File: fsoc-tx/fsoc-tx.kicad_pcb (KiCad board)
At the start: 4 copper layers, 52 x 40 mm, 52 parts, among them J1 USB4105-GF-A, J2 B8B-PH-K-S, J3 FTSH-105-01-L-DV-K, J4 B3B-PH-K-S, J5 Conn_01x03, SW1 SW_RESET, SW2 USB_BOOT, SW3 SW_DPST, U1 USBLC6-2SC6, U2 AP2112K-3.3, U3 RP2354A, U4 74AHCT1G125, U5 TPS22919DCK, Y1 ABM8-272-T3, Y2 ASTX-H11-10.000MHz-T

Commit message: TX PCB: DONE
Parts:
- J1: footprint Connector_USB:USB_C_Receptacle_GCT_USB4105-xx-A_16P_TopMnt_Horizontal -> fsoc_footprints:TYPE-C-31-M-14
- moved J1 2.44 mm to (150.9, 106.0)
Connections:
- net /USB_DM renamed /USB_DN
- net Net-(J1-D+-PadA6) renamed /TX_POWER_USB/USB_CONN_DP
- net Net-(J1-D--PadA7) renamed /TX_POWER_USB/USB_CONN_DN
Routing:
- net GND: track 102.7 -> 98.5 mm, vias 53 -> 47
- net /TX_POWER_USB/USB_CONN_DP: track 11.3 -> 13.0 mm
- net /USB_DN: track 2.87 -> 4.38 mm
- net Net-(J1-CC2): track 4.43 -> 5.76 mm
- net /TX_POWER_USB/USB_CONN_DN: track 11.2 -> 12.1 mm
- net Net-(J1-CC1): track 3.20 -> 4.13 mm
- net /TX_POWER_USB/VBUS_USB: track 42.9 -> 43.6 mm, vias 0 -> 2
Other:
- board size 52 x 40 mm -> 52.1 x 40 mm

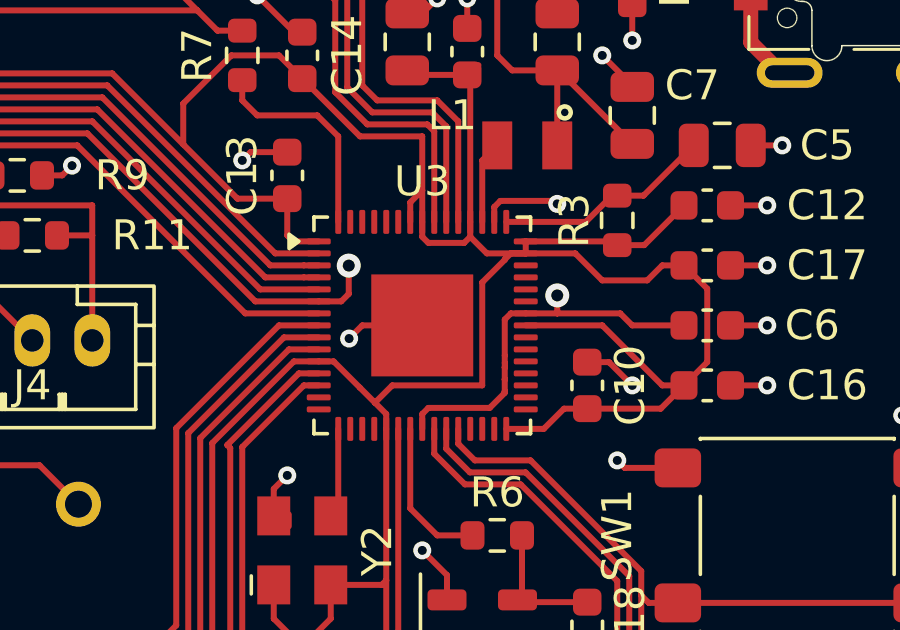
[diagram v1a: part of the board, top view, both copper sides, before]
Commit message: TX PCB: U3 footprint changed to the thermal vias version
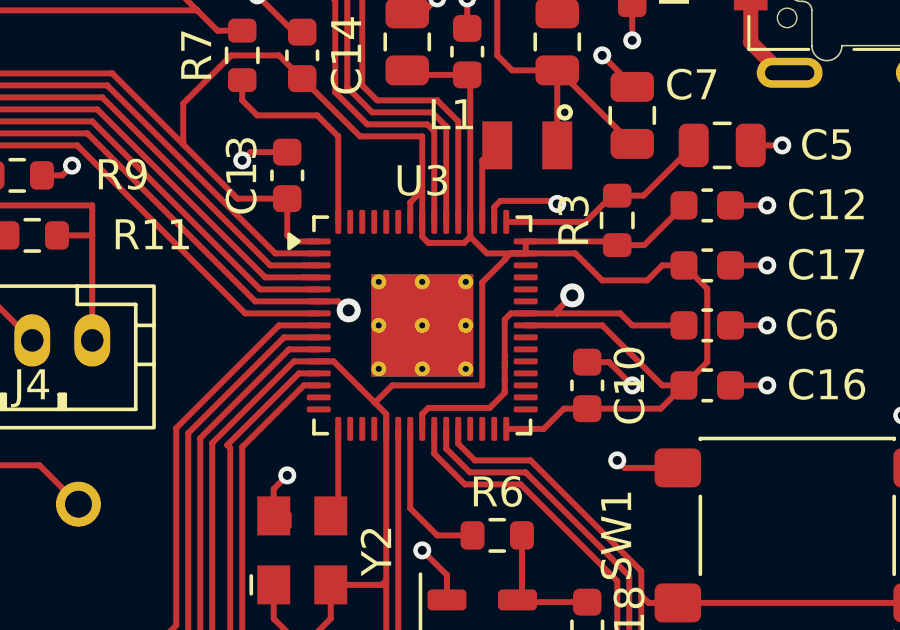
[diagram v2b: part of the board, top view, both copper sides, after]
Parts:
- U3: footprint Package_DFN_QFN:QFN-60-1EP_7x7mm_P0.4mm_EP3.4x3.4mm -> Package_DFN_QFN:QFN-60-1EP_7x7mm_P0.4mm_EP3.4x3.4mm_ThermalVias
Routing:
- net /TX_MCU_CLOCK/+1V1: track 84.1 -> 87.0 mm
- net GND: track 98.5 -> 95.9 mm, vias 47 -> 46
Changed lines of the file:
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@@
 		)
 	)
-	(footprint "Package_DFN_QFN:QFN-60-1EP_7x7mm_P0.4mm_EP3.4x3.4mm"
+	(footprint "Package_DFN_QFN:QFN-60-1EP_7x7mm_P0.4mm_EP3.4x3.4mm_ThermalVias"
 		(layer "F.Cu")
 		(at 135 120)
@@
 		)
 		(pad "" smd roundrect
-			(at -1.13 -1.13)
-			(size 0.91 0.91)
+			(at -0.85 -0.85)
+			(size 1.32 1.32)
 			(layers "F.Paste")
-			(roundrect_rratio 0.25)
-		)
-		(pad "" smd roundrect
-			(at -1.13 0)
-			(size 0.91 0.91)
-			(layers "F.Paste")
-			(roundrect_rratio 0.25)
-		)
-		(pad "" smd roundrect
-			(at -1.13 1.13)
-			(size 0.91 0.91)
-			(layers "F.Paste")
-			(roundrect_rratio 0.25)
-		)
-		(pad "" smd roundrect
-			(at 0 -1.13)
-			(size 0.91 0.91)
-			(layers "F.Paste")
-			(roundrect_rratio 0.25)
-		)
-		(pad "" smd roundrect
-			(at 0 0)
-			(size 0.91 0.91)
-			(layers "F.Paste")
-			(roundrect_rratio 0.25)
-		)
-		(pad "" smd roundrect
-			(at 0 1.13)
-			(size 0.91 0.91)
-			(layers "F.Paste")
-			(roundrect_rratio 0.25)
+			(roundrect_rratio 0.189394)
 		)
 		(pad "" smd roundrect
-			(at 1.13 -1.13)
-			(size 0.91 0.91)
+			(at -0.85 0.85)
+			(size 1.32 1.32)
 			(layers "F.Paste")
-			(roundrect_rratio 0.25)
+			(roundrect_rratio 0.189394)
 		)
 		(pad "" smd roundrect
-			(at 1.13 0)
-			(size 0.91 0.91)
+			(at 0.85 -0.85)
+			(size 1.32 1.32)
 			(layers "F.Paste")
-			(roundrect_rratio 0.25)
+			(roundrect_rratio 0.189394)
 		)
 		(pad "" smd roundrect
-			(at 1.13 1.13)
-			(size 0.91 0.91)
+			(at 0.85 0.85)
+			(size 1.32 1.32)
 			(layers "F.Paste")
-			(roundrect_rratio 0.25)
+			(roundrect_rratio 0.189394)
 		)
 		(pad "1" smd roundrect
@@
 			(pintype "output")
 		)
+		(pad "61" thru_hole circle
+			(at -1.45 -1.45)
+			(size 0.5 0.5)
+			(drill 0.2)
+			(property pad_prop_heatsink)
+			(layers "*.Cu")
+			(remove_unused_layers no)
+			(net "GND")
+			(pinfunction "GND_61")
+			(pintype "power_in")
+		)
+		(pad "61" thru_hole circle
+			(at -1.45 0)
+			(size 0.5 0.5)
+			(drill 0.2)
+			(property pad_prop_heatsink)
+			(layers "*.Cu")
+			(remove_unused_layers no)
+			(net "GND")
+			(pinfunction "GND_61")
+			(pintype "power_in")
+		)
+		(pad "61" thru_hole circle
+			(at -1.45 1.45)
+			(size 0.5 0.5)
+			(drill 0.2)
+			(property pad_prop_heatsink)
+			(layers "*.Cu")
+			(remove_unused_layers no)
+			(net "GND")
+			(pinfunction "GND_61")
+			(pintype "power_in")
+		)
+		(pad "61" thru_hole circle
+			(at 0 -1.45)
+			(size 0.5 0.5)
+			(drill 0.2)
+			(property pad_prop_heatsink)
+			(layers "*.Cu")
+			(remove_unused_layers no)
+			(net "GND")
+			(pinfunction "GND_61")
+			(pintype "power_in")
+		)
+		(pad "61" thru_hole circle
+			(at 0 0)
+			(size 0.5 0.5)
+			(drill 0.2)
+			(property pad_prop_heatsink)
+			(layers "*.Cu")
+			(remove_unused_layers no)
+			(net "GND")
+			(pinfunction "GND_61")
+			(pintype "power_in")
+		)
 		(pad "61" smd rect
 			(at 0 0)
@@
 			(zone_connect 2)
 		)
+		(pad "61" smd rect
+			(at 0 0)
+			(size 3.4 3.4)
+			(property pad_prop_heatsink)
+			(layers "B.Cu")
+			(net "GND")
+			(pinfunction "GND_61")
+			(pintype "power_in")
+			(zone_connect 2)
+		)
+		(pad "61" thru_hole circle
+			(at 0 1.45)
+			(size 0.5 0.5)
+			(drill 0.2)
+			(property pad_prop_heatsink)
+			(layers "*.Cu")
+			(remove_unused_layers no)
+			(net "GND")
+			(pinfunction "GND_61")
+			(pintype "power_in")
+		)
+		(pad "61" thru_hole circle
+			(at 1.45 -1.45)
+			(size 0.5 0.5)
+			(drill 0.2)
+			(property pad_prop_heatsink)
+			(layers "*.Cu")
+			(remove_unused_layers no)
+			(net "GND")
+			(pinfunction "GND_61")
+			(pintype "power_in")
+		)
+		(pad "61" thru_hole circle
+			(at 1.45 0)
+			(size 0.5 0.5)
+			(drill 0.2)
+			(property pad_prop_heatsink)
+			(layers "*.Cu")
+			(remove_unused_layers no)
+			(net "GND")
+			(pinfunction "GND_61")
+			(pintype "power_in")
+		)
+		(pad "61" thru_hole circle
+			(at 1.45 1.45)
+			(size 0.5 0.5)
+			(drill 0.2)
+			(property pad_prop_heatsink)
+			(layers "*.Cu")
+			(remove_unused_layers no)
+			(net "GND")
+			(pinfunction "GND_61")
+			(pintype "power_in")
+		)
 		(embedded_fonts no)
 		(model "${KICAD10_3DMODEL_DIR}/Package_DFN_QFN.3dshapes/QFN-60-1EP_7x7mm_P0.4mm_EP3.4x3.4mm.step"
@@
 	)
 	(segment
-		(start 132.562089 120.437911)
-		(end 133 120)
-		(width 0.2)
-		(layer "F.Cu")
-		(net "GND")
-	)
-	(segment
 		(start 145.95 101.483946)
 		(end 147.083946 100.35)
@@
 	)
 	(segment
-		(start 133 120)
-		(end 135 120)
-		(width 0.2)
-		(layer "F.Cu")
-		(net "GND")
-	)
-	(segment
 		(start 141.225 121.225)
 		(end 142 122)
@@
 	)
 	(via
-		(at 132.562089 120.437911)
-		(size 0.6)
-		(drill 0.3)
-		(layers "F.Cu" "B.Cu")
-		(net "GND")
-	)
-	(via
 		(at 147 114)
 		(size 0.6)
@@
 	)
 	(segment
-		(start 132.3 119.2)
-		(end 131.55 119.2)
-		(width 0.2)
-		(layer "F.Cu")
-		(net "/TX_MCU_CLOCK/+1V1")
-	)
-	(segment
 		(start 137.75364 121.4)
 		(end 137.75 121.39636)
@@
 	)
 	(segment
-		(start 132.55 118.95)
-		(end 132.3 119.2)
-		(width 0.2)
-		(layer "F.Cu")
-		(net "/TX_MCU_CLOCK/+1V1")
-	)
-	(segment
 		(start 137.75364 122.2)
 		(end 137.75 122.19636)
@@
 	)
 	(segment
+		(start 132.501163 119.498837)
+		(end 132.548216 119.498837)
+		(width 0.2)
+		(layer "F.Cu")
+		(net "/TX_MCU_CLOCK/+1V1")
+	)
+	(segment
 		(start 131.55 119.2)
 		(end 129.437256 119.2)
@@
 	)
 	(segment
+		(start 132.5 119.5)
+		(end 132.501163 119.498837)
+		(width 0.2)
+		(layer "F.Cu")
+		(net "/TX_MCU_CLOCK/+1V1")
+	)
+	(segment
 		(start 133.5 112.5)
 		(end 133 112)
@@
 	)
 	(segment
-		(start 139.5 119.6)
-		(end 139.5 119)
+		(start 131.55 119.2)
+		(end 132.2 119.2)
 		(width 0.2)
 		(layer "F.Cu")
@@
 	)
 	(segment
+		(start 139.5 119.5)
+		(end 140 119)
+		(width 0.2)
+		(layer "F.Cu")
+		(net "/TX_MCU_CLOCK/+1V1")
+	)
+	(segment
+		(start 132.2 119.2)
+		(end 132.5 119.5)
+		(width 0.2)
+		(layer "F.Cu")
+		(net "/TX_MCU_CLOCK/+1V1")
+	)
+	(segment
 		(start 133 109)
 		(end 133.5 108.5)
@@
 	)
 	(segment
+		(start 139.5 119.6)
+		(end 139.5 119.5)
+		(width 0.2)
+		(layer "F.Cu")
+		(net "/TX_MCU_CLOCK/+1V1")
+	)
+	(segment
 		(start 137.75 121.40364)
 		(end 137.75364 121.4)
@@
 	)
 	(segment
-		(start 132.55 118.006761)
-		(end 132.55 118.95)
-		(width 0.2)
-		(layer "F.Cu")
-		(net "/TX_MCU_CLOCK/+1V1")
-	)
-	(segment
 		(start 137.75 122.19636)
 		(end 137.75 121.80364)
@@
 	)
 	(via
-		(at 139.5 119)
+		(at 132.548216 119.498837)
 		(size 0.8)
 		(drill 0.4)
@@
 	)
 	(via
-		(at 132.55 118.006761)
+		(at 140 119)
 		(size 0.8)
 		(drill 0.4)
@@
 	)
 	(segment
-		(start 133.5 118)
-		(end 132.556761 118)
+		(start 132.548216 115)
+		(end 132.548216 108.451784)
 		(width 0.5)
 		(layer "In2.Cu")
@@
 	)
 	(segment
-		(start 132.556761 118)
-		(end 132.55 118.006761)
+		(start 132.548216 108.451784)
+		(end 133.5 107.5)
 		(width 0.5)
 		(layer "In2.Cu")
@@
 	)
 	(segment
-		(start 133.5 118)
-		(end 138.5 118)
+		(start 132.548216 119.498837)
+		(end 132.548216 115)
 		(width 0.5)
 		(layer "In2.Cu")
@@
 	)
 	(segment
-		(start 138.5 118)
-		(end 139.5 119)
+		(start 136 115)
+		(end 140 119)
 		(width 0.5)
 		(layer "In2.Cu")
@@
 	)
 	(segment
-		(start 133.5 107.5)
-		(end 133.5 118)
+		(start 132.548216 115)
+		(end 136 115)
 		(width 0.5)
 		(layer "In2.Cu")

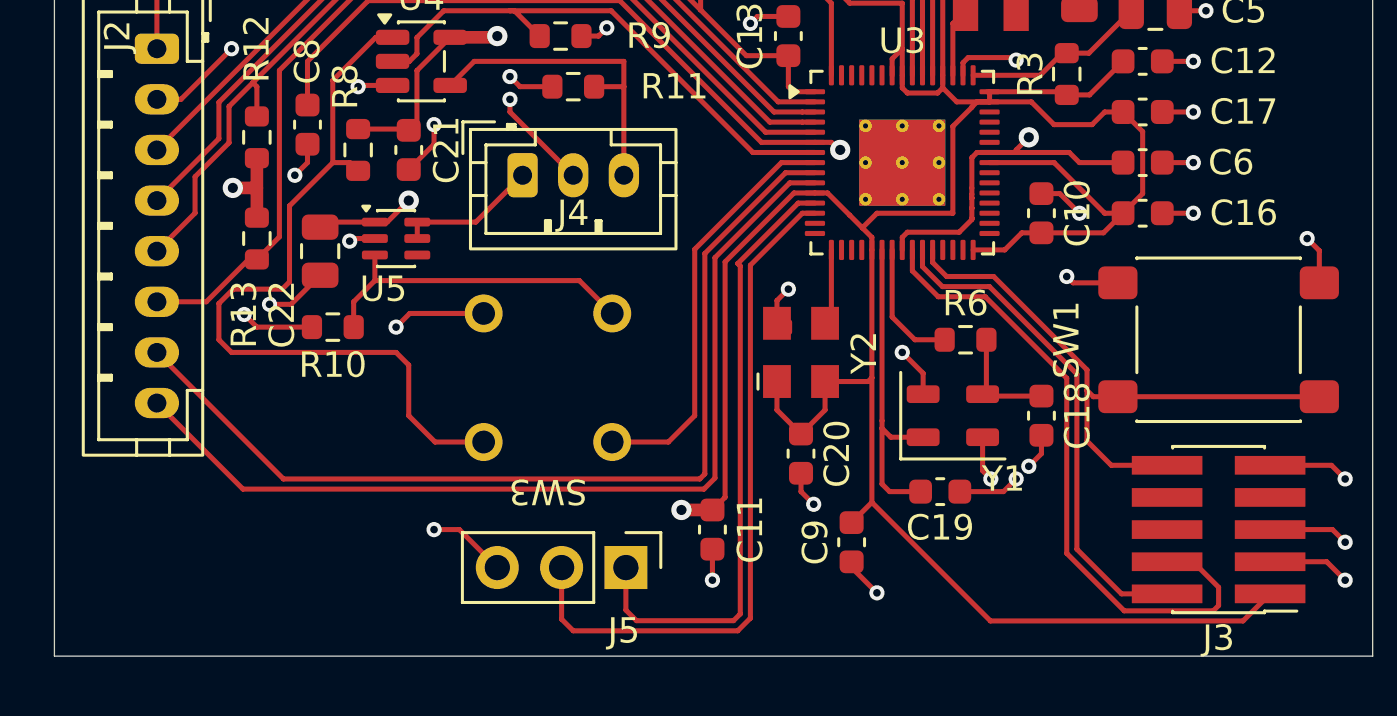
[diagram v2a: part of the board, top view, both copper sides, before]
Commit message: Switching ASTX-H11 to SiT5346 and SiT5346 datasheet
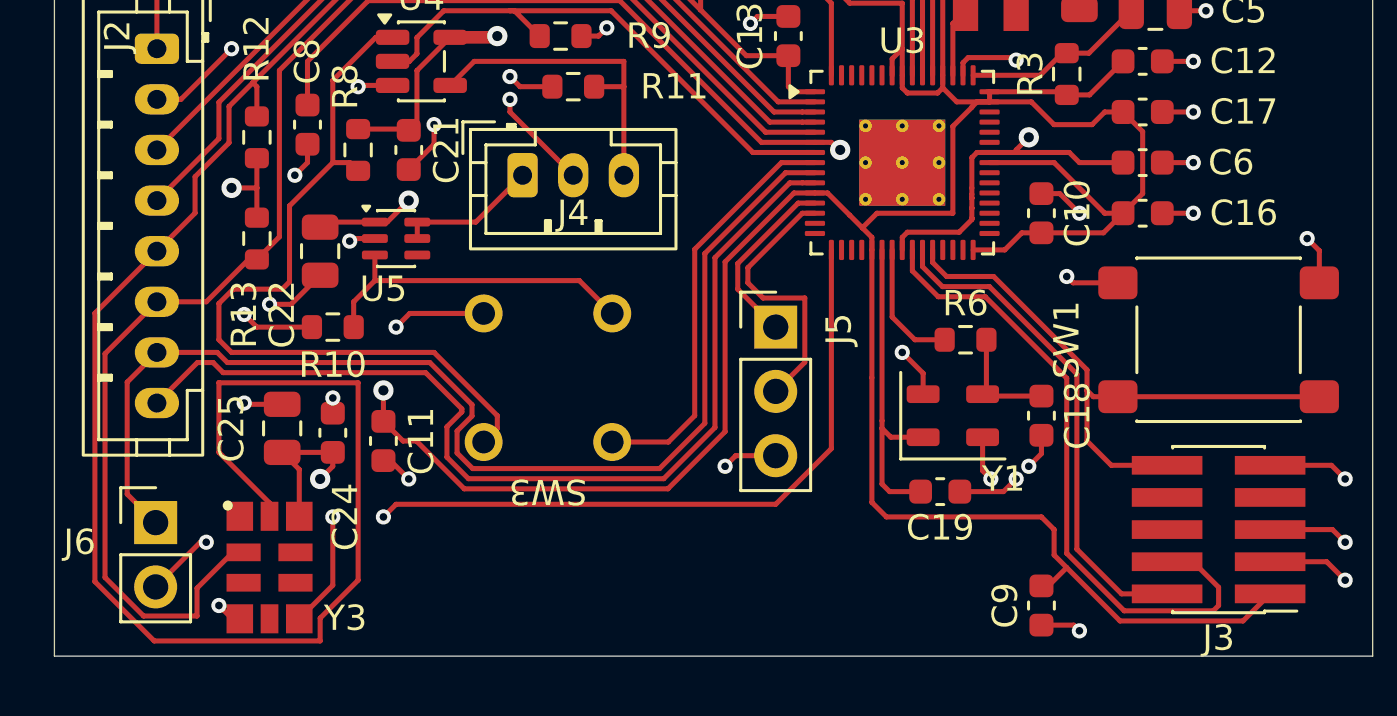
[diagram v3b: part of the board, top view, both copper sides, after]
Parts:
- removed C20: 10 nF, Capacitor_SMD:C_0603_1608Metric
- removed Y2: ASTX-H11-10.000MHz-T, fsoc_footprints:ASTX-H11_3225
- added C24: 100 nF, Capacitor_SMD:C_0603_1608Metric, F.Cu at (112.5, 130.7)
- added C25: 10 µF, Capacitor_SMD:C_0805_2012Metric, F.Cu at (110.5, 130.5)
- added J6: Conn_01x02, Connector_PinHeader_2.54mm:PinHeader_1x02_P2.54mm_Vertical, F.Cu at (105.5, 134.2)
- added Y3: SiT5346, fsoc_footprints:SiT5346_5.0x3.2mm_10L, F.Cu at (110.0, 136.0)
- moved C11 13.5 mm to (114.5, 131.0)
- moved J5 11.2 mm to (130.0, 126.5), turned to 0 degrees
- moved C9 7.91 mm to (140.5, 137.5)
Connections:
- U3 pad 16: /TX_MCU_CLOCK/TCXO_10M -> /TX_MCU_CLOCK/REF_10M
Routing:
- net /HOST_I2C_SDA: track 35.8 -> 82.2 mm
- net /TX_MCU_CLOCK/REF_10M: track 0.00 -> 33.2 mm, vias 0 -> 2
- net /HOST_I2C_SCL: track 37.3 -> 56.8 mm
- net /UART_DEBUG_TX: track 24.4 -> 7.17 mm
- net /UART_DEBUG_RX: track 27.2 -> 10.8 mm
- net /PPS_OUT: track 38.2 -> 46.3 mm
- net /TX_MCU_CLOCK/TCXO_10M: track 3.00 -> 0.00 mm
- net /+3V3_DIG: track 180.2 -> 177.9 mm, vias 2 -> 3
- net /HOST_READY: track 38.0 -> 39.7 mm
- net GND: track 95.9 -> 97.3 mm, vias 46 -> 48

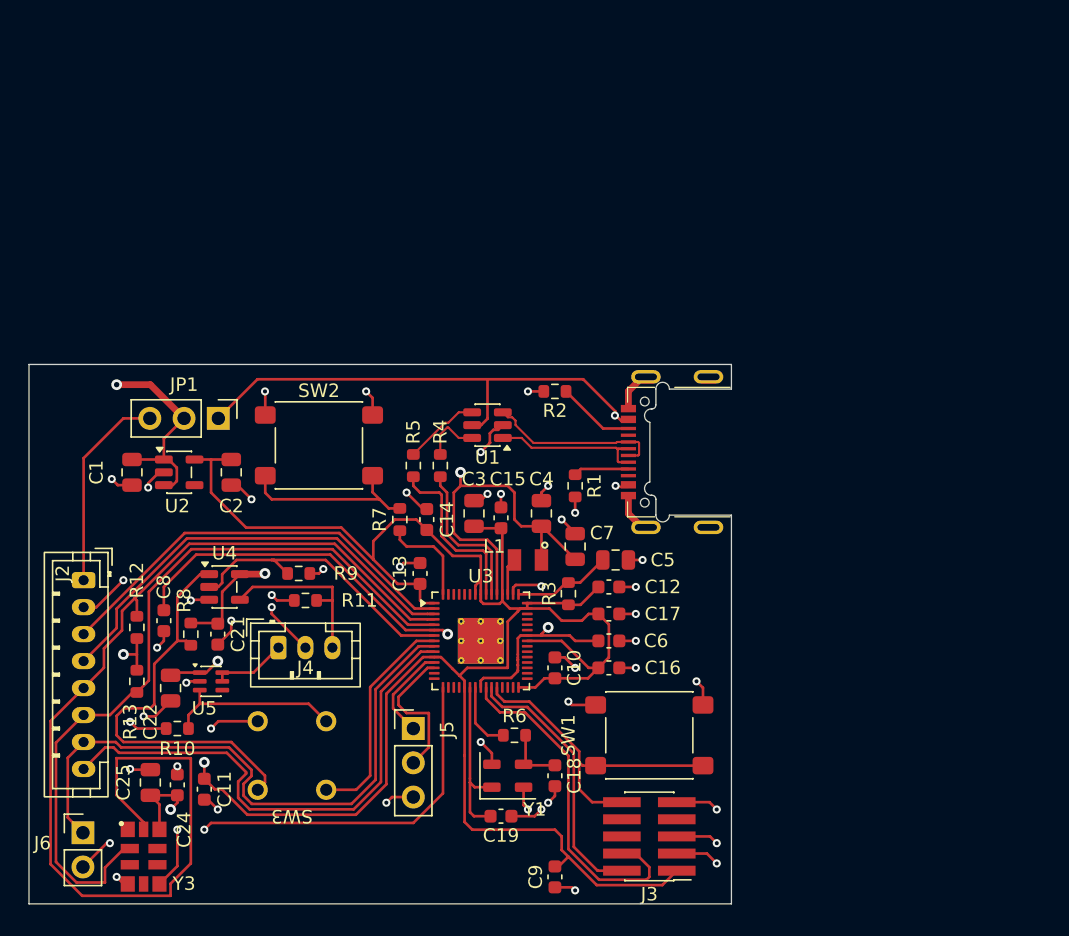
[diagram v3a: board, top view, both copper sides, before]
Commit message: SiT5346 ordering code updated
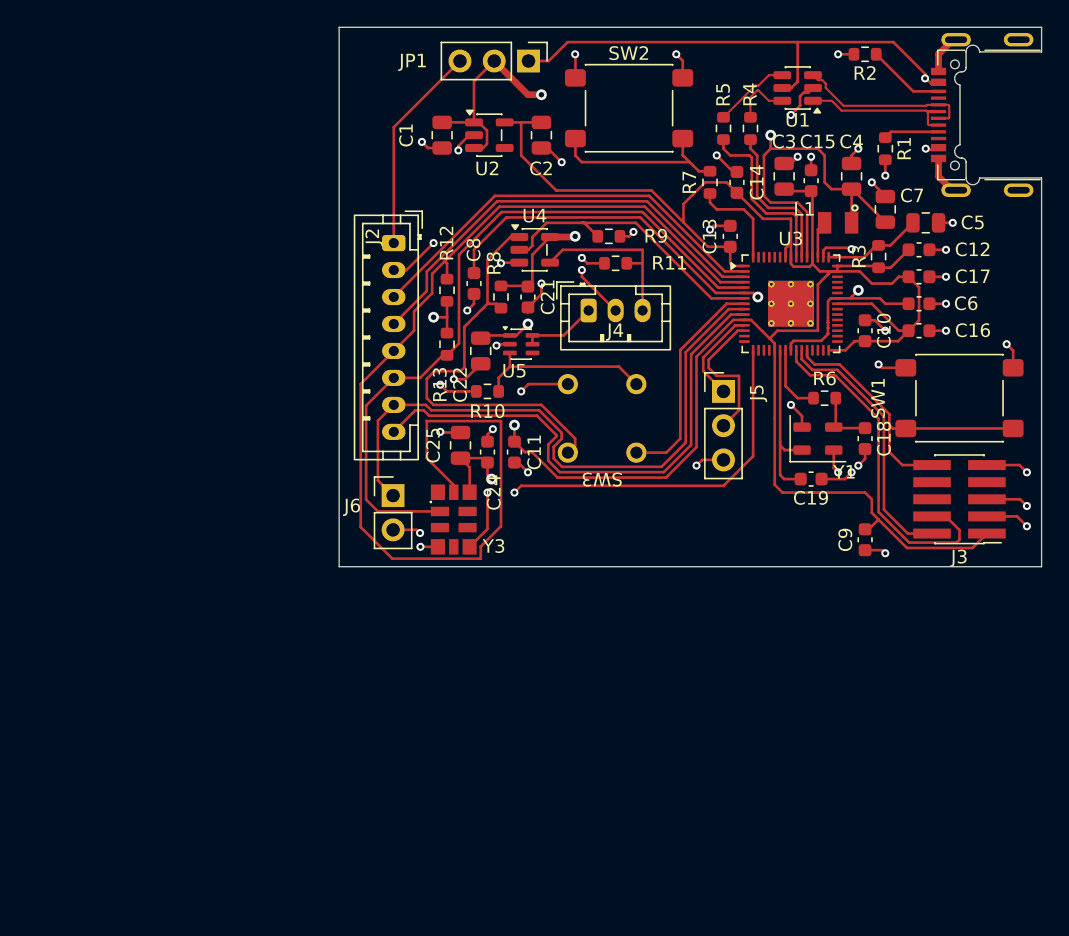
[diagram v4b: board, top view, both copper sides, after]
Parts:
- moved JP1 35.1 mm to (138.5, 77.0)
- moved J2 34.0 mm to (128.6, 90.5)
- moved C10 34.0 mm to (163.5, 97.0)
- moved C11 34.0 mm to (137.5, 106.0)
- moved C12 34.0 mm to (167.5, 91.0)
- moved C13 34.0 mm to (153.5, 90.0)
- moved C14 34.0 mm to (154.0, 86.0)
- moved C15 34.0 mm to (159.5, 85.9)
- moved C16 34.0 mm to (167.5, 97.0)
- moved C17 34.0 mm to (167.5, 93.0)
- moved C18 34.0 mm to (163.5, 105.0)
- moved C19 34.0 mm to (159.5, 108.0)
- moved C2 34.0 mm to (139.5, 82.5)
- moved C21 34.0 mm to (138.5, 94.5)
- moved C22 34.0 mm to (135.0, 98.5)
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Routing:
- net /SYS_5V: track 59.7 -> 47.6 mm
- net /HOST_I2C_SCL: track 56.8 -> 53.0 mm
- net /+3V3_DIG: track 177.9 -> 178.8 mm
- net /TX_POWER_USB/VBUS_USB: track 43.6 -> 43.0 mm
- net GND: track 97.3 -> 97.9 mm

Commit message: manufacturing files
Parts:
- J2: footprint Connector_JST:JST_PH_B8B-PH-K_1x08_P2.00mm_Vertical -> Connector_PinHeader_2.54mm:PinHeader_1x08_P2.54mm_Vertical
- J4: footprint Connector_JST:JST_PH_B3B-PH-K_1x03_P2.00mm_Vertical -> Connector_PinHeader_2.54mm:PinHeader_1x03_P2.54mm_Vertical
- moved J2 3.33 mm to (127.5, 87.3), turned to 0 degrees
- moved J4 0.51 mm to (142.9, 96.0), turned to 90 degrees
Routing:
- net /TX_POWER_USB/VIN_HOST_5V: track 15.5 -> 12.8 mm
- net /HOST_I2C_SCL: track 53.0 -> 54.6 mm
- net /PPS_OUT: track 46.3 -> 47.7 mm
- net GND: track 97.9 -> 99.1 mm
- net /TX_LASER/LASER_DATA_5V: track 12.9 -> 13.8 mm
- net /HOST_READY: track 39.7 -> 40.6 mm
